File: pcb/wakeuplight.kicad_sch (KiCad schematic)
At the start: 27 parts, among them J1 691322310002, J31 Conn_01x19, J32 Conn_01x19, J7 MPT 2,54, J8 MPT 2,54, Q2 T2N7002BK, SW1 SW_Push, SW2 SW_Push, SW3 SW_Push, SW4 SW_Push

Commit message: work on PCB: line out + power done ; removed amplifier from board
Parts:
- added H1, H2, H3, H4: MountingHole, MountingHole:MountingHole_3.2mm_M3_DIN965, symbol Mechanical:MountingHole
- added J13: USB_A, Connector_USB:USB_A_TE_292303-7_Horizontal, symbol Connector:USB_A
- added JP11: SolderJumper_2_Bridged, Jumper:SolderJumper-2_P1.3mm_Bridged_Pad1.0x1.5mm, symbol Jumper:SolderJumper_2_Bridged
- SW3: renamed from SW2; now left out of the parts list
- renumbered C2 to C1, C10 to C2, J7 to J4, J8 to J5, R8 to R1, R1 to R2, R9 to R3, R7 to R4, R6 to R5, R2 to R6, R10 to R7, SW3 to SW2, TP3 to TP1, TP1 to TP2, TP2 to TP3, TP5 to TP4, TP4 to TP5
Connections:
- net +5V: now also J13.1 (VBUS)
- net GND: now also J13.4 (GND), JP11.2 (B)
- new net: J13.5 (Shield), JP11.1 (A)
- no-connect marks 19 -> 22
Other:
- sheet MAX98357A ports: added I2S_DIN; removed I2S_DOUT
- sheet PCM5102A ports: added BCK, DIN, LCK; removed none

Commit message: PCB done
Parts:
- added H7: MountingHole, MountingHole:MountingHole_3.2mm_M3_DIN965, symbol Mechanical:MountingHole
- added JP12: SolderJumper_2_Open, Jumper:SolderJumper-2_P1.3mm_Open_Pad1.0x1.5mm, symbol Jumper:SolderJumper_2_Open
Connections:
- net +5V: no longer J13.1 (VBUS)
- net EN_bottom: now also J32.6 (Pin_6); no longer J32.8 (Pin_8)
- net EN_top: now also J32.8 (Pin_8); no longer J32.6 (Pin_6)
- net GND: now also J31.3 (Pin_3), J31.4 (Pin_4), J31.5 (Pin_5), J31.6 (Pin_6), J31.7 (Pin_7)
- net regulator_5v_audio/~{SHDN}: now reaches Q2.2 (S)
- net mute: now reaches J32.15 (Pin_15)
- net mute: now also JP12.1 (A)
- net ~{EN}_audio renamed EN_audio
- new net 5V_audio: J13.1 (VBUS)
- new net PCM5102A/XMT: JP12.2 (B)
- no-connect marks 22 -> 17
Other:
- added sheet regulator_5v_audio (regulator_5v.kicad_sch)
- sheet PCM5102A ports: added XMT; removed none
- sheet regulator_5v ports: added ~{SHDN}; removed none
- note removed: "TODO: - single FET to diable 5V for speakers - line-out jack: LRG"
- moved on the sheet: J13, JP11, Q2, R1

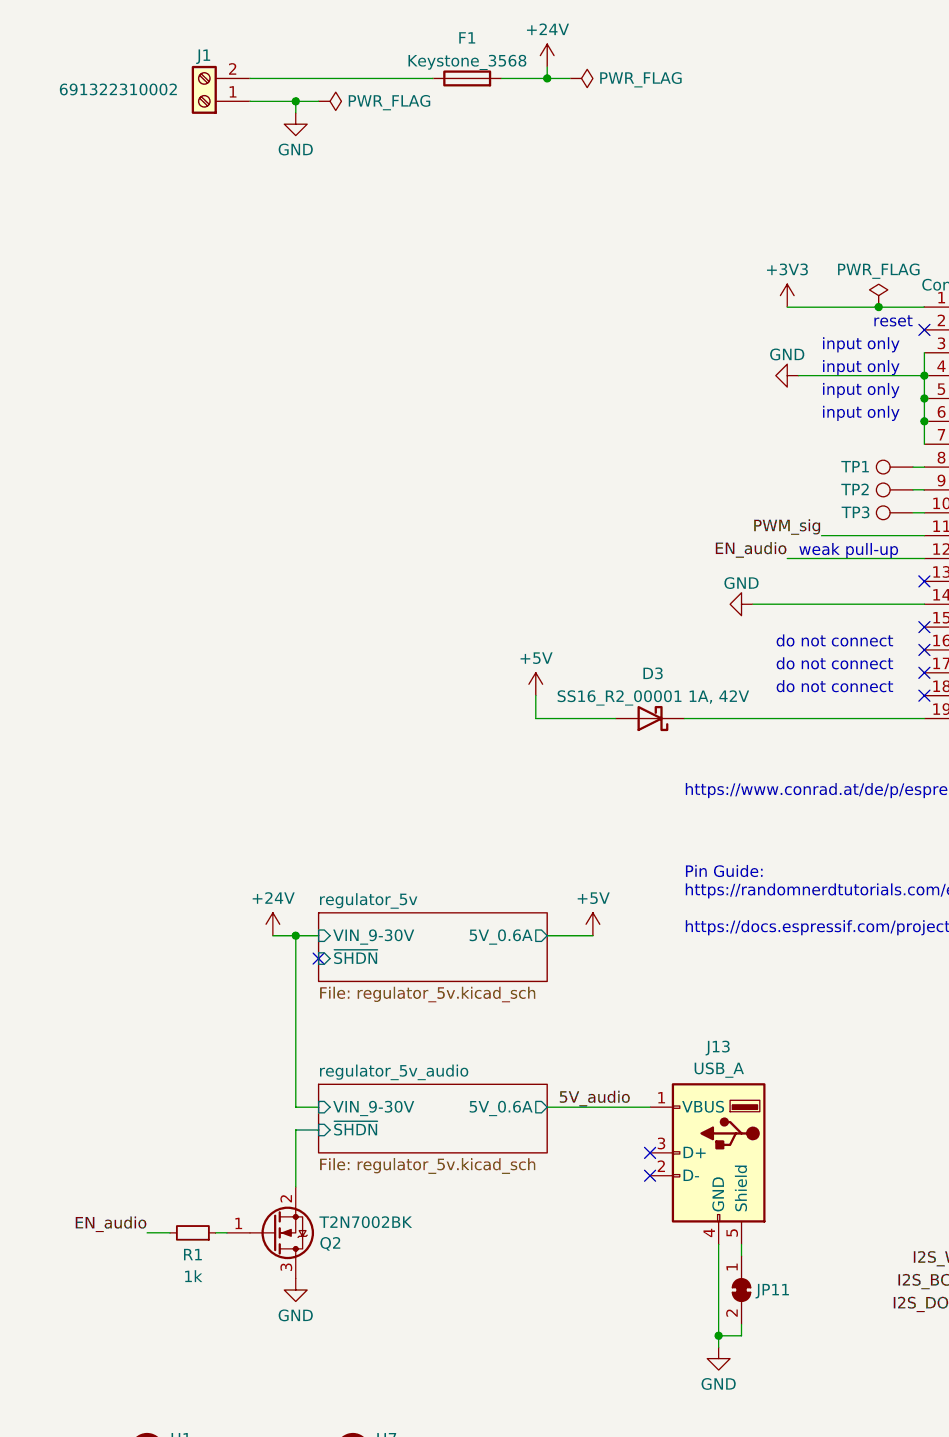
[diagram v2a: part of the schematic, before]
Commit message: PCB: renamed "EN_audio" to "~EN_audio" ; added input capacitor (PSU noise) ; fixed mirrored MOSFET
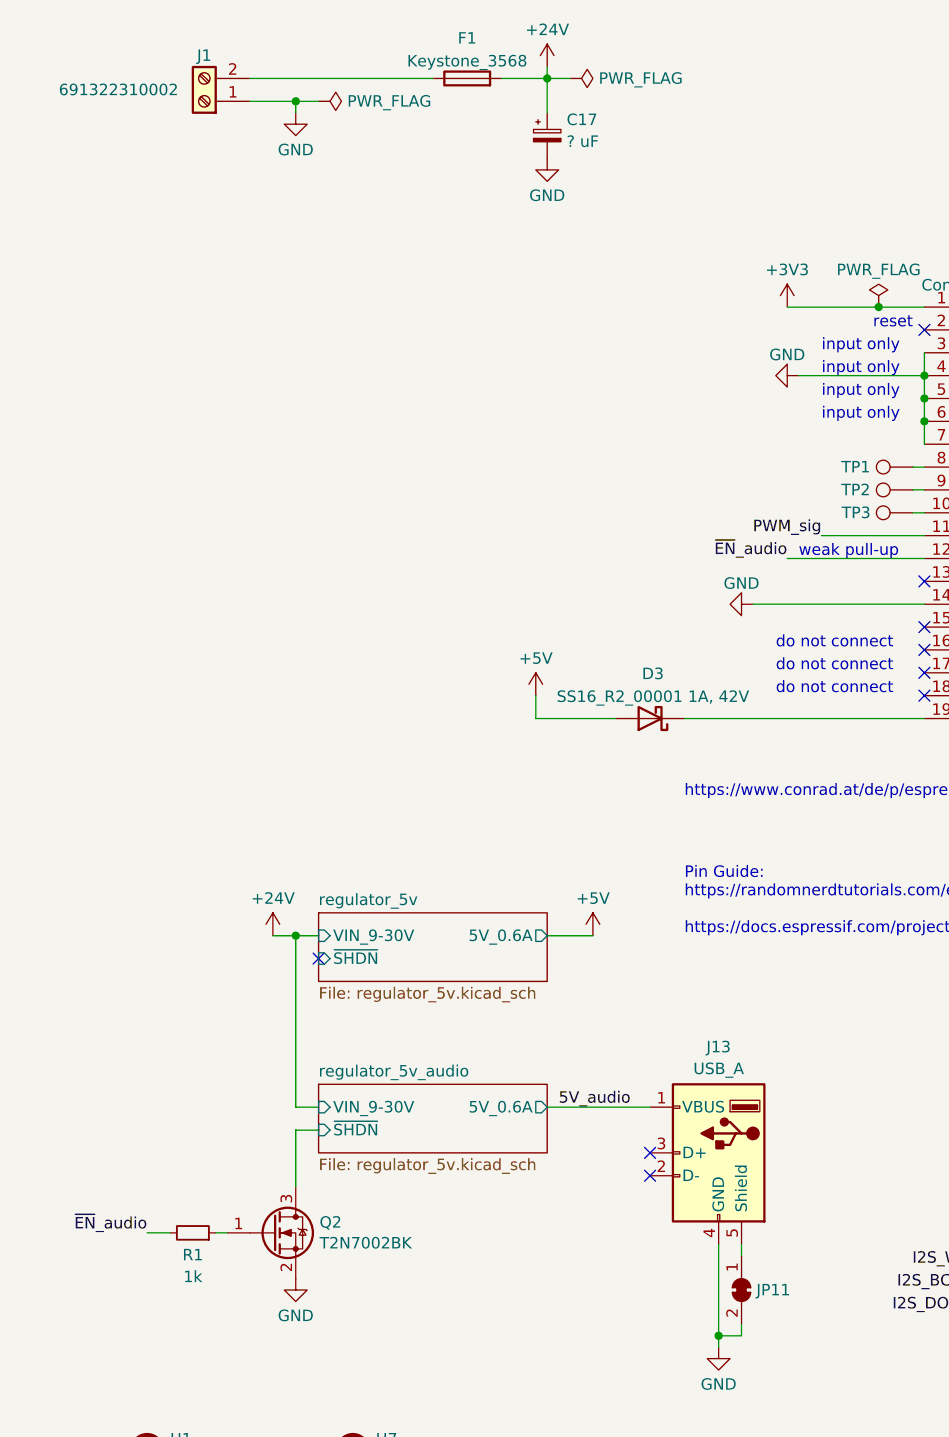
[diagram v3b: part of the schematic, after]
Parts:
- added C17: ? uF, Capacitor_THT:CP_Radial_D10.0mm_P5.00mm, symbol Device:C_Polarized_Small
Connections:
- net +24V: now also C17.1
- net GND: now also Q2.2 (S), C17.2; no longer Q2.3 (D)
- net regulator_5v_audio/~{SHDN}: now also Q2.3 (D); no longer Q2.2 (S)
- net EN_audio renamed ~{EN}_audio
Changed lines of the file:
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@@
+    (stroke (width 0) (type default))
+  )
+  (wire (pts (xy 68.58 24.13) (xy 68.58 27.94))
     (stroke (width 0) (type default))
   )
@@
     (effects (font (size 1.27 1.27)) (justify left bottom))
   )
-  (label "EN_audio" (at 24.13 152.4 180) (fields_autoplaced)
+  (label "~{EN}_audio" (at 24.13 152.4 180) (fields_autoplaced)
     (effects (font (size 1.27 1.27)) (justify right bottom))
   )
@@
     (effects (font (size 1.27 1.27)) (justify left bottom))
   )
-  (label "EN_audio" (at 95.25 77.47 180) (fields_autoplaced)
+  (label "~{EN}_audio" (at 95.25 77.47 180) (fields_autoplaced)
     (effects (font (size 1.27 1.27)) (justify right bottom))
   )
@@
     )
   )
+  (symbol (lib_id "power:GND") (at 68.58 33.02 0) (unit 1)
+    (in_bom yes) (on_board yes) (dnp no) (fields_autoplaced)
+    (property "Reference" "#PWR065" (at 68.58 39.37 0)
+      (effects (font (size 1.27 1.27)) hide)
+    )
+    (property "Value" "GND" (at 68.58 37.1531 0)
+      (effects (font (size 1.27 1.27)))
+    )
+    (property "Footprint" "" (at 68.58 33.02 0)
+      (effects (font (size 1.27 1.27)) hide)
+    )
+    (property "Datasheet" "" (at 68.58 33.02 0)
+      (effects (font (size 1.27 1.27)) hide)
+    )
+    (pin "1")
+    (instances
+      (project "wakeuplight"
+        (path "/f5441fcc-7db8-443c-8d47-1d2e67dbd624"
+          (reference "#PWR065") (unit 1)
+        )
+      )
+    )
+  )
   (symbol (lib_id "Connector:TestPoint") (at 109.22 69.85 90) (unit 1)
     (in_bom yes) (on_board yes) (dnp no)
@@
     )
   )
-  (symbol (lib_id "Transistor_FET:DMN10H220L") (at 38.1 152.4 0) (mirror x) (unit 1)
+  (symbol (lib_id "Transistor_FET:DMN10H220L") (at 38.1 152.4 0) (unit 1)
     (in_bom yes) (on_board yes) (dnp no)
-    (property "Reference" "Q2" (at 43.2816 153.5684 0)
-      (effects (font (size 1.27 1.27)) (justify left))
-    )
-    (property "Value" "T2N7002BK" (at 43.2816 151.257 0)
-      (effects (font (size 1.27 1.27)) (justify left))
-    )
-    (property "Footprint" "Package_TO_SOT_SMD:SOT-23" (at 43.18 150.495 0)
+    (property "Reference" "Q2" (at 43.2816 151.2316 0)
+      (effects (font (size 1.27 1.27)) (justify left))
+    )
+    (property "Value" "T2N7002BK" (at 43.2816 153.543 0)
+      (effects (font (size 1.27 1.27)) (justify left))
+    )
+    (property "Footprint" "Package_TO_SOT_SMD:SOT-23" (at 43.18 154.305 0)
       (effects (font (size 1.27 1.27) italic) (justify left) hide)
     )
@@
         )
       )
+    )
+  )
+  (symbol (lib_id "Device:C_Polarized_Small") (at 68.58 30.48 0) (unit 1)
+    (in_bom yes) (on_board yes) (dnp no) (fields_autoplaced)
+    (property "Reference" "C17" (at 70.739 28.7218 0)
+      (effects (font (size 1.27 1.27)) (justify left))
+    )
+    (property "Value" "? uF" (at 70.739 31.146 0)
+      (effects (font (size 1.27 1.27)) (justify left))
+    )
+    (property "Footprint" "Capacitor_THT:CP_Radial_D10.0mm_P5.00mm" (at 68.58 30.48 0)
+      (effects (font (size 1.27 1.27)) hide)
+    )
+    (property "Datasheet" "~" (at 68.58 30.48 0)
+      (effects (font (size 1.27 1.27)) hide)
+    )
+    (pin "2")
+    (pin "1")
+    (instances
+      (project "wakeuplight"
+        (path "/f5441fcc-7db8-443c-8d47-1d2e67dbd624"
+          (reference "C17") (unit 1)
+        )
+      )

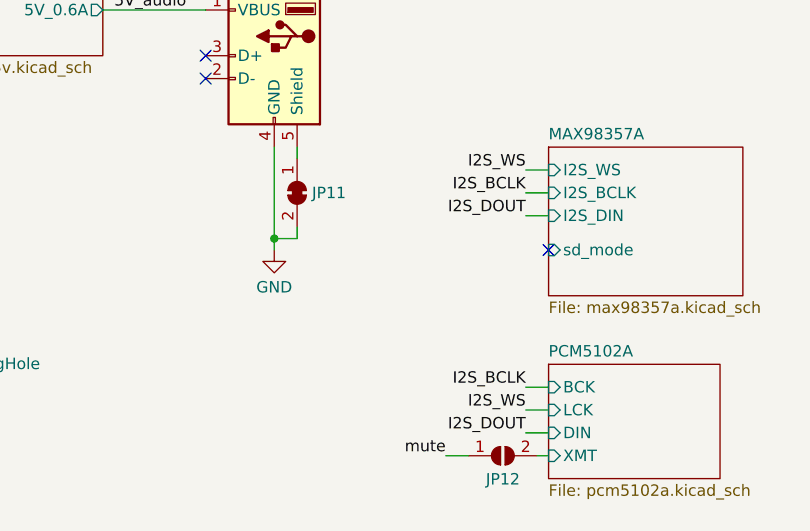
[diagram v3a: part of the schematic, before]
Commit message: moved to Kicad 8
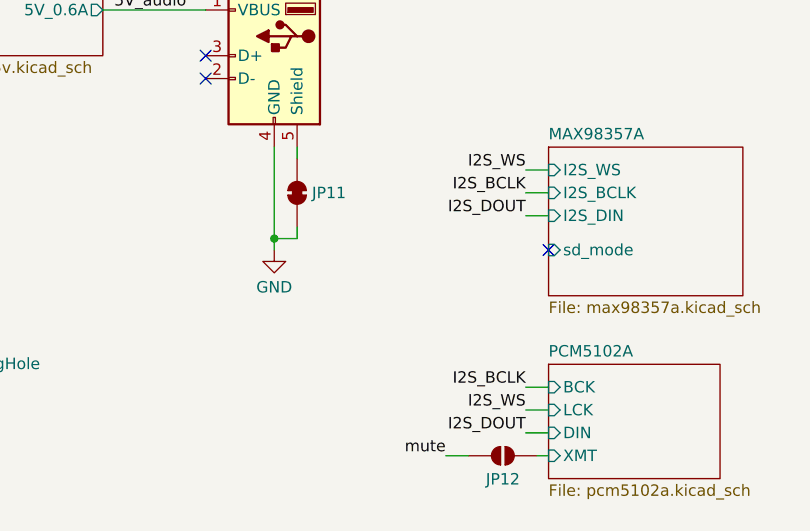
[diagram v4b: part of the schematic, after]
